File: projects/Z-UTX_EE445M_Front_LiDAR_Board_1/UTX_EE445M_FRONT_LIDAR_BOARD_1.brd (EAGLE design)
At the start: 100.5 x 51.7 mm, 5 parts, among them IC1 EK-TM4C123GXLP

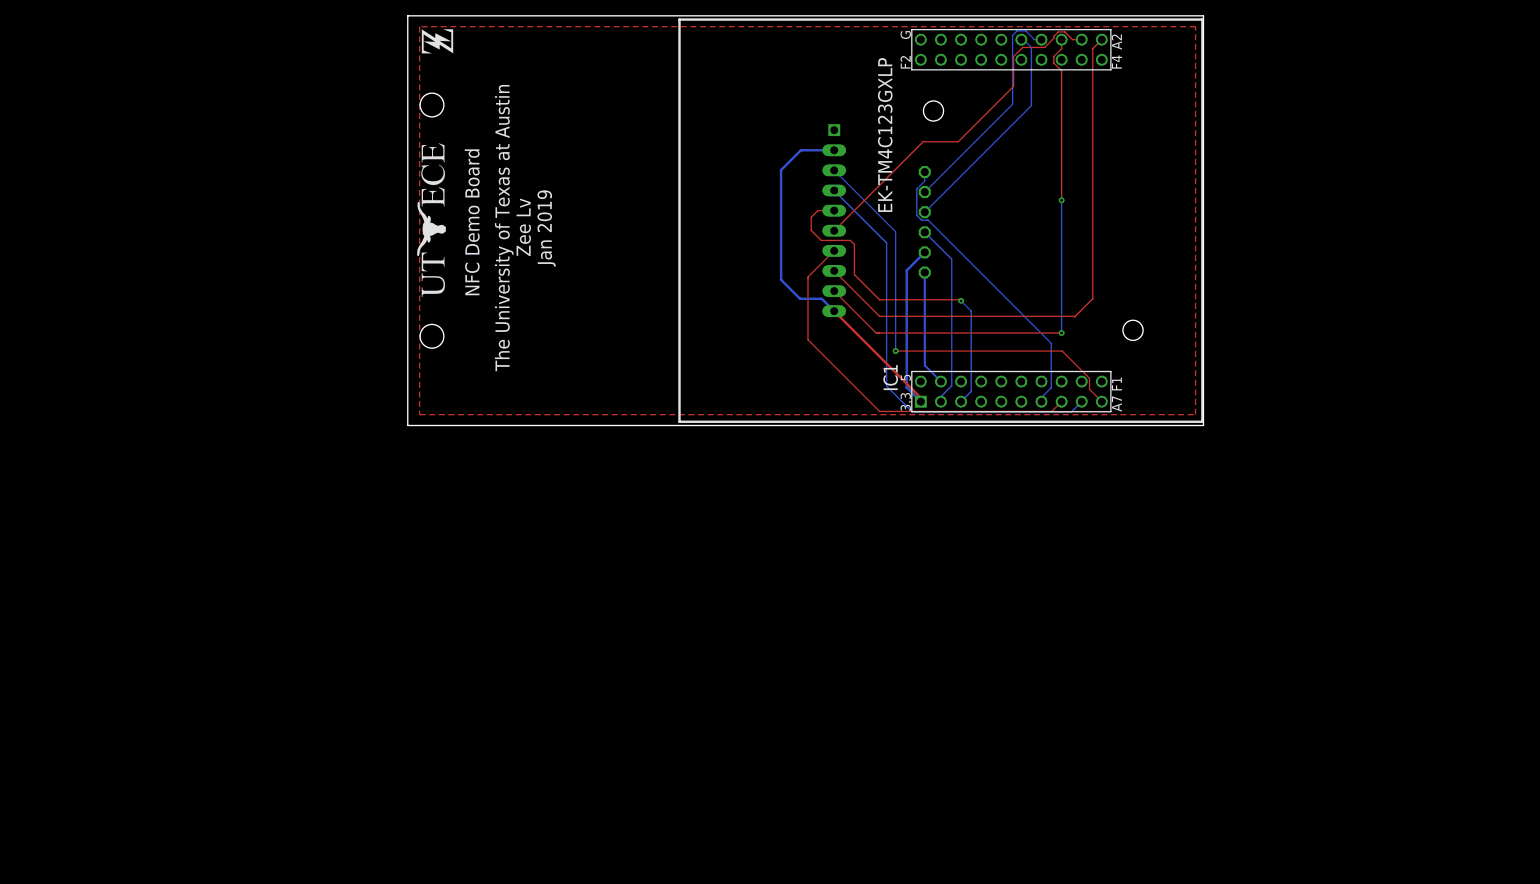
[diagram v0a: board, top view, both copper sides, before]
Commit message: add 2 new designs of UTexas EE445M front LiDAR board
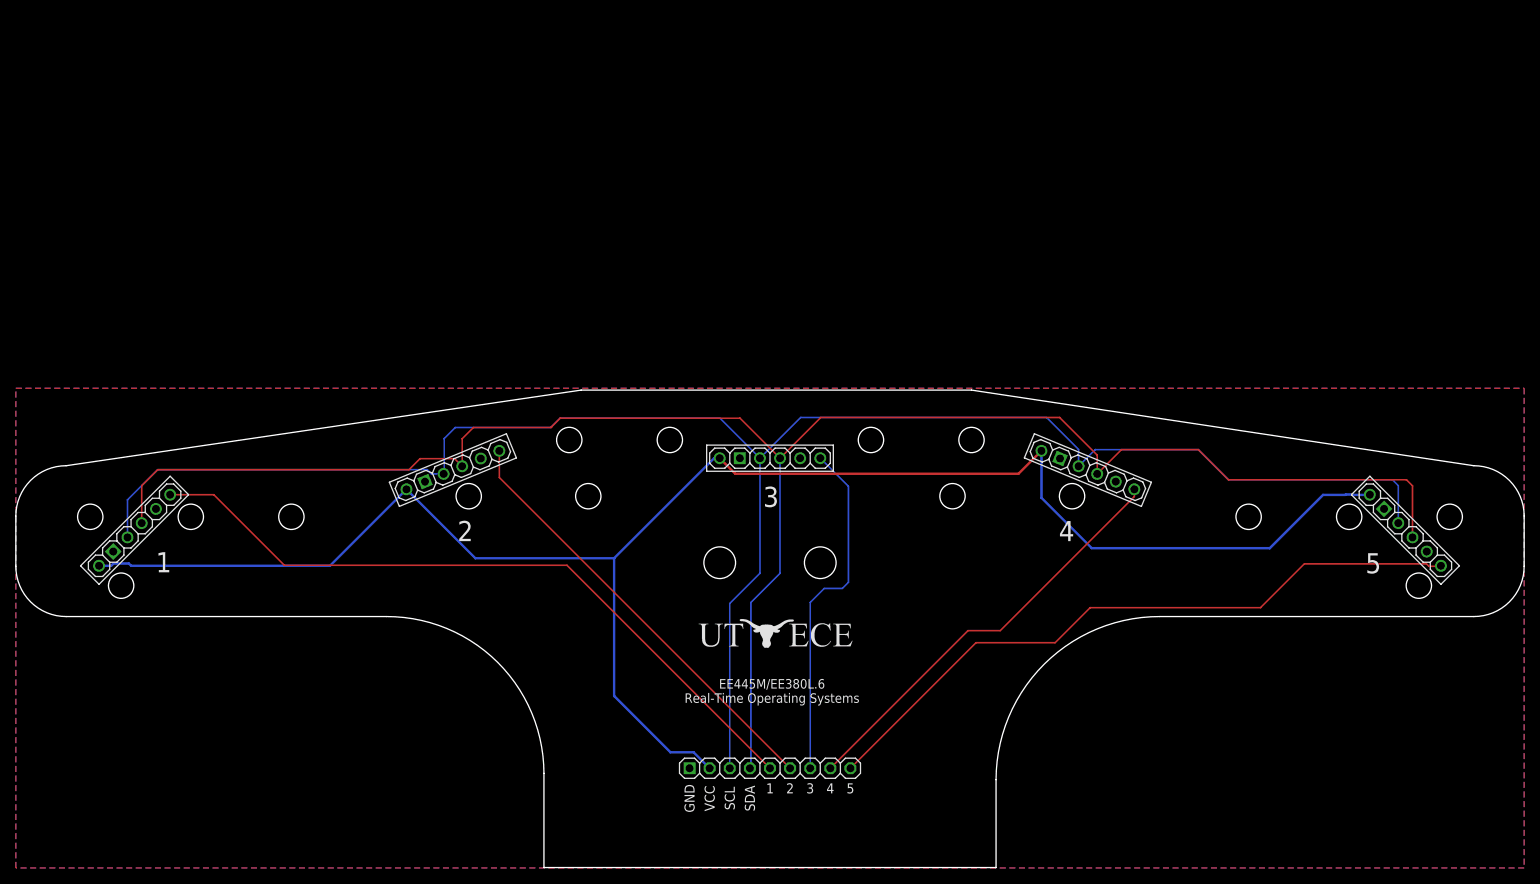
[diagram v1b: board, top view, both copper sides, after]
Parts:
- removed DIS1: ST7735, UT_ECE:ST7735
- removed IC1: EK-TM4C123GXLP, UT_ECE:TM4C123LAUNCHPAD
- added U$4, U$5, U$6: LIDAR_VL53L0X_ATK_VERT, Z:LIDAR_VL53L0X_ATK_VERT
- added U$7: (no value), Z:LOGO_UT_ECE_20X4
- added U$8: (no value), Z:LOGO_Z_3X4
- U$1: value ELECHOUSE_PN532_SPI -> UTX_EE445M_LIDAR_FRONT_BOARD_CONNECTOR_PTH; device Z:ELECHOUSE_PN532_SPI -> Z:UTX_EE445M_LIDAR_FRONT_BOARD_CONNECTOR_PTH
- U$2: value (none) -> LIDAR_VL53L0X_ATK_VERT; device Z:LOGO_UT_ECE_20X4 -> Z:LIDAR_VL53L0X_ATK_VERT
- U$3: value (none) -> LIDAR_VL53L0X_ATK_VERT; device Z:LOGO_Z_3X4 -> Z:LIDAR_VL53L0X_ATK_VERT
- moved U$1 79.0 mm to (95.2, -21.7), flipped to the top, turned to 0 degrees
- moved U$3 52.6 mm to (55.2, 18.5), turned to 22.5 degrees
- moved U$2 49.1 mm to (15.0, 10.9), turned to 45 degrees
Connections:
- removed net 3V3: DIS1.10, DIS1.2, IC1.1, U$1.VCC
- removed net 5V: IC1.21
- removed net SD_CS: DIS1.5, IC1.3
- removed net SSI0_MISO: DIS1.9, IC1.13
- removed net SSI0_MOSI: DIS1.7, IC1.8
- removed net SSI0_SCK: DIS1.8, IC1.11
- removed net SSI0_SS: DIS1.6, IC1.12
- removed net SSI2_MISO: IC1.14, U$1.MISO
- removed net SSI2_MOSI: IC1.15, U$1.MOSI
- removed net SSI2_SCK: IC1.7, U$1.SCK
- removed net SSI2_SS: IC1.2, U$1.SS
- removed net ST7735_DC: DIS1.4, IC1.9
- removed net ST7735_RESET: DIS1.3, IC1.10
- new net N$1: U$3.INT
- new net N$13: U$2.INT
- new net N$2: U$6.INT
- new net N$3: U$4.INT
- new net N$5: U$5.INT
- new net SCL: U$1.SCL, U$2.SCL, U$3.SCL, U$4.SCL, U$5.SCL, U$6.SCL
- new net SDA: U$1.SDA, U$2.SDA, U$3.SDA, U$4.SDA, U$5.SDA, U$6.SDA
- new net VCC: U$1.VCC, U$2.VCC, U$3.VCC, U$4.VCC, U$5.VCC, U$6.VCC
- new net XSHUT1: U$1.XSHUT1, U$2.XSH
- new net XSHUT2: U$1.XSHUT2, U$3.XSH
- new net XSHUT3: U$1.XSHUT3, U$4.XSH
- new net XSHUT4: U$1.XSHUT4, U$5.XSH
- new net XSHUT5: U$1.XSHUT5, U$6.XSH
- net GND: now also U$2.GND, U$3.GND, U$4.GND, U$5.GND, U$6.GND; no longer DIS1.1, IC1.20, IC1.22
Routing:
- net SDA: track 0.00 -> 230.6 mm
- net SCL: track 0.00 -> 228.8 mm
- net VCC: track 0.00 -> 220.2 mm
- net XSHUT1: track 0.00 -> 90.1 mm
- net XSHUT5: track 0.00 -> 85.4 mm
- net SSI0_SCK: track 69.2 -> 0.00 mm
- net SSI0_MISO: track 68.8 -> 0.00 mm, vias 2 -> 0
- net 3V3: track 66.5 -> 0.00 mm
- net ST7735_RESET: track 55.5 -> 0.00 mm, vias 1 -> 0
- net XSHUT2: track 0.00 -> 55.3 mm
- net ST7735_DC: track 54.0 -> 0.00 mm
- net XSHUT4: track 0.00 -> 53.5 mm
- net SSI0_MOSI: track 48.9 -> 0.00 mm
- net SSI0_SS: track 44.4 -> 0.00 mm
- net XSHUT3: track 0.00 -> 44.0 mm
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- added copper zone on layer 16, net GND
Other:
- board size 100.5 x 51.7 mm -> 190.5 x 60.3 mm
- board text added: "1"
- board text added: "2"
- board text added: "3"
- board text added: "4"
- board text added: "5"
- board text added: "EE445M/EE380L.6 Real-Time Operating Systems"
- board text added: "University of Texas at Austin Zee Lv, Sijin Woo March 2019"
- board text removed: "NFC Demo Board"
- board text removed: "The University of Texas at Austin Zee Lv Jan 2019"

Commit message: fixed some tiny inperfections
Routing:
- net VCC: track 220.2 -> 218.1 mm
- net XSHUT3: track 44.0 -> 42.5 mm
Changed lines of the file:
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@@
 <contactref element="U$5" pad="VCC"/>
 <contactref element="U$6" pad="VCC"/>
-<wire x1="87.63" y1="-19.16" x2="85.615" y2="-17.145" width="0.3048" layer="16"/>
-<wire x1="85.615" y1="-17.145" x2="82.677" y2="-17.145" width="0.3048" layer="16"/>
-<wire x1="82.677" y1="-17.145" x2="75.565" y2="-10.033" width="0.3048" layer="16"/>
-<wire x1="75.565" y1="-10.033" x2="75.565" y2="7.366" width="0.3048" layer="16"/>
+<wire x1="87.63" y1="-19.16" x2="75.565" y2="-7.095" width="0.3048" layer="16"/>
+<wire x1="75.565" y1="-7.095" x2="75.565" y2="7.366" width="0.3048" layer="16"/>
 <wire x1="75.565" y1="7.366" x2="88.199" y2="20" width="0.3048" layer="16"/>
 <wire x1="88.199" y1="20" x2="88.9" y2="20" width="0.3048" layer="16"/>
@@
 <wire x1="90.866" y1="18.034" x2="126.637325" y2="18.034" width="0.3048" layer="1"/>
 <wire x1="129.5333625" y1="20.9300375" x2="129.5333625" y2="14.9926375" width="0.3048" layer="16"/>
-<wire x1="129.5333625" y1="14.9926375" x2="135.89" y2="8.636" width="0.3048" layer="16"/>
-<wire x1="135.89" y1="8.636" x2="158.369" y2="8.636" width="0.3048" layer="16"/>
-<wire x1="158.369" y1="8.636" x2="165.1" y2="15.367" width="0.3048" layer="16"/>
-<wire x1="170.986746875" y1="15.367" x2="171.009871875" y2="15.390125" width="0.3048" layer="16"/>
-<wire x1="165.1" y1="15.367" x2="167.93045" y2="15.367" width="0.3048" layer="16"/>
-<wire x1="168.86955" y1="15.367" x2="170.986746875" y2="15.367" width="0.3048" layer="16"/>
-<wire x1="167.93045" y1="15.367" x2="167.96995" y2="15.4065" width="0.3048" layer="16"/>
-<wire x1="167.96995" y1="15.4065" x2="168.83005" y2="15.4065" width="0.3048" layer="16"/>
-<wire x1="168.83005" y1="15.4065" x2="168.86955" y2="15.367" width="0.3048" layer="16"/>
+<wire x1="129.5333625" y1="14.9926375" x2="135.255" y2="9.271" width="0.3048" layer="16"/>
+<wire x1="135.255" y1="9.271" x2="159.004" y2="9.271" width="0.3048" layer="16"/>
+<wire x1="159.004" y1="9.271" x2="165.227" y2="15.494" width="0.3048" layer="16"/>
+<wire x1="171.009871875" y1="15.390125" x2="170.905996875" y2="15.494" width="0.3048" layer="16"/>
+<wire x1="170.905996875" y1="15.494" x2="165.227" y2="15.494" width="0.3048" layer="16"/>
 </signal>
 <signal name="SCL">
@@
 <wire x1="56.373325" y1="18.98600625" x2="56.373325" y2="22.464325" width="0.2032" layer="1"/>
 <wire x1="56.373325" y1="22.464325" x2="57.785" y2="23.876" width="0.2032" layer="1"/>
-<wire x1="57.785" y1="23.876" x2="67.619890625" y2="23.876" width="0.2032" layer="1"/>
-<wire x1="67.619890625" y1="23.876" x2="67.652334375" y2="23.90844375" width="0.2032" layer="1"/>
-<wire x1="67.652334375" y1="23.90844375" x2="67.652334375" y2="23.964365625" width="0.2032" layer="1"/>
-<wire x1="67.652334375" y1="23.964365625" x2="68.74366875" y2="25.0557" width="0.2032" layer="1"/>
+<wire x1="57.785" y1="23.876" x2="67.56396875" y2="23.876" width="0.2032" layer="1"/>
+<wire x1="67.56396875" y1="23.876" x2="68.74366875" y2="25.0557" width="0.2032" layer="1"/>
 <wire x1="91.4643" y1="25.0557" x2="96.52" y2="20" width="0.2032" layer="1"/>
 <wire x1="68.74366875" y1="25.0557" x2="91.4643" y2="25.0557" width="0.2032" layer="1"/>
@@
 <contactref element="U$1" pad="XSHUT1"/>
 <contactref element="U$2" pad="XSH"/>
-<wire x1="95.25" y1="-19.16" x2="69.613" y2="6.477" width="0.2032" layer="1"/>
+<wire x1="95.25" y1="-19.16" x2="69.74" y2="6.35" width="0.2032" layer="1"/>
 <wire x1="24.995875" y1="15.390125" x2="19.490125" y2="15.390125" width="0.2032" layer="1"/>
-<wire x1="69.613" y1="6.477" x2="33.909" y2="6.477" width="0.2032" layer="1"/>
-<wire x1="33.909" y1="6.477" x2="24.995875" y2="15.390125" width="0.2032" layer="1"/>
+<wire x1="69.74" y1="6.35" x2="34.036" y2="6.35" width="0.2032" layer="1"/>
+<wire x1="34.036" y1="6.35" x2="24.995875" y2="15.390125" width="0.2032" layer="1"/>
 </signal>
 <signal name="XSHUT2">
@@
 <contactref element="U$4" pad="XSH"/>
 <contactref element="U$1" pad="XSHUT3"/>
-<wire x1="100.33" y1="-19.16" x2="100.33" y2="1.778" width="0.2032" layer="16"/>
-<wire x1="100.33" y1="1.778" x2="102.108" y2="3.556" width="0.2032" layer="16"/>
-<wire x1="102.108" y1="3.556" x2="104.394" y2="3.556" width="0.2032" layer="16"/>
-<wire x1="104.394" y1="3.556" x2="105.156" y2="4.318" width="0.2032" layer="16"/>
-<wire x1="105.156" y1="16.444" x2="101.6" y2="20" width="0.2032" layer="16"/>
-<wire x1="105.156" y1="4.318" x2="105.156" y2="16.444" width="0.2032" layer="16"/>
+<wire x1="100.33" y1="-19.16" x2="100.33" y2="-0.508" width="0.2032" layer="16"/>
+<wire x1="100.33" y1="-0.508" x2="105.029" y2="4.191" width="0.2032" layer="16"/>
+<wire x1="105.029" y1="16.571" x2="101.6" y2="20" width="0.2032" layer="16"/>
+<wire x1="105.029" y1="4.191" x2="105.029" y2="16.571" width="0.2032" layer="16"/>
 </signal>
 <signal name="XSHUT4">
@@
 <contactref element="U$6" pad="XSH"/>
 <wire x1="105.41" y1="-19.16" x2="121.268" y2="-3.302" width="0.2032" layer="1"/>
-<wire x1="131.263934375" y1="-3.302" x2="135.688140625" y2="1.12220625" width="0.2032" layer="1"/>
-<wire x1="135.688140625" y1="1.12220625" x2="157.20520625" y2="1.12220625" width="0.2032" layer="1"/>
-<wire x1="121.268" y1="-3.302" x2="131.263934375" y2="-3.302" width="0.2032" layer="1"/>
+<wire x1="125.167934375" y1="-3.302" x2="135.379634375" y2="6.9097" width="0.2032" layer="1"/>
+<wire x1="135.379634375" y1="6.9097" x2="177.908171875" y2="6.9097" width="0.2032" layer="1"/>
+<wire x1="121.268" y1="-3.302" x2="125.167934375" y2="-3.302" width="0.2032" layer="1"/>
 <wire x1="179.930253125" y1="6.35" x2="179.990125" y2="6.409871875" width="0.2032" layer="1"/>
 <wire x1="178.467871875" y1="6.35" x2="179.930253125" y2="6.35" width="0.2032" layer="1"/>
-<wire x1="178.162171875" y1="6.6557" x2="178.467871875" y2="6.35" width="0.2032" layer="1"/>
-<wire x1="162.7387" y1="6.6557" x2="178.162171875" y2="6.6557" width="0.2032" layer="1"/>
-<wire x1="157.20520625" y1="1.12220625" x2="162.7387" y2="6.6557" width="0.2032" layer="1"/>
+<wire x1="177.908171875" y1="6.9097" x2="178.467871875" y2="6.35" width="0.2032" layer="1"/>
 </signal>
 <signal name="N$13">
